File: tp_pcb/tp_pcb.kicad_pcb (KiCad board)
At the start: 2 copper layers, 66.5 x 76 mm, 23 parts, among them K0 KEYSW, K1 KEYSW, K2 KEYSW, K3 KEYSW, K4 KEYSW, K5 KEYSW, K6 KEYSW, P0 CONN_01X08, P1 CONN_01X08, P2 CONN_01X06

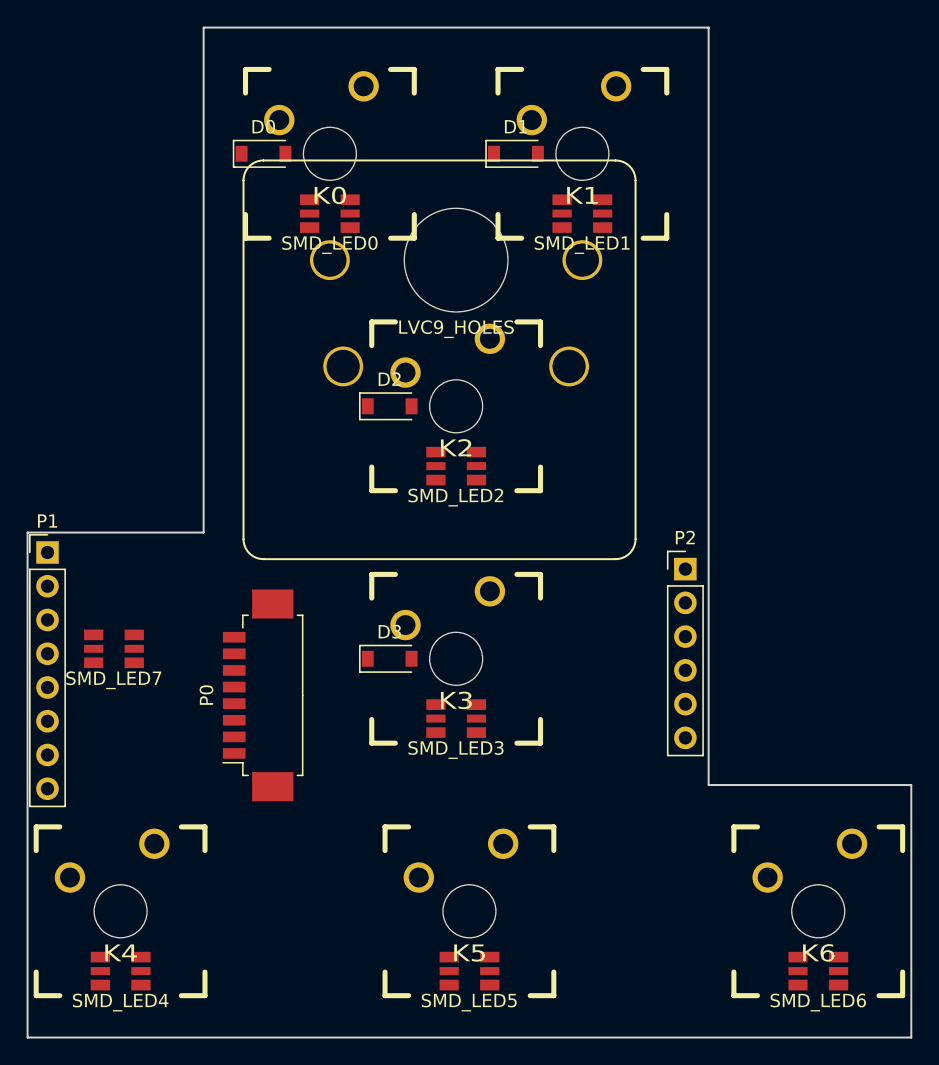
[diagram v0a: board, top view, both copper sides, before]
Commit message: tp_pcb routing, woo interactive
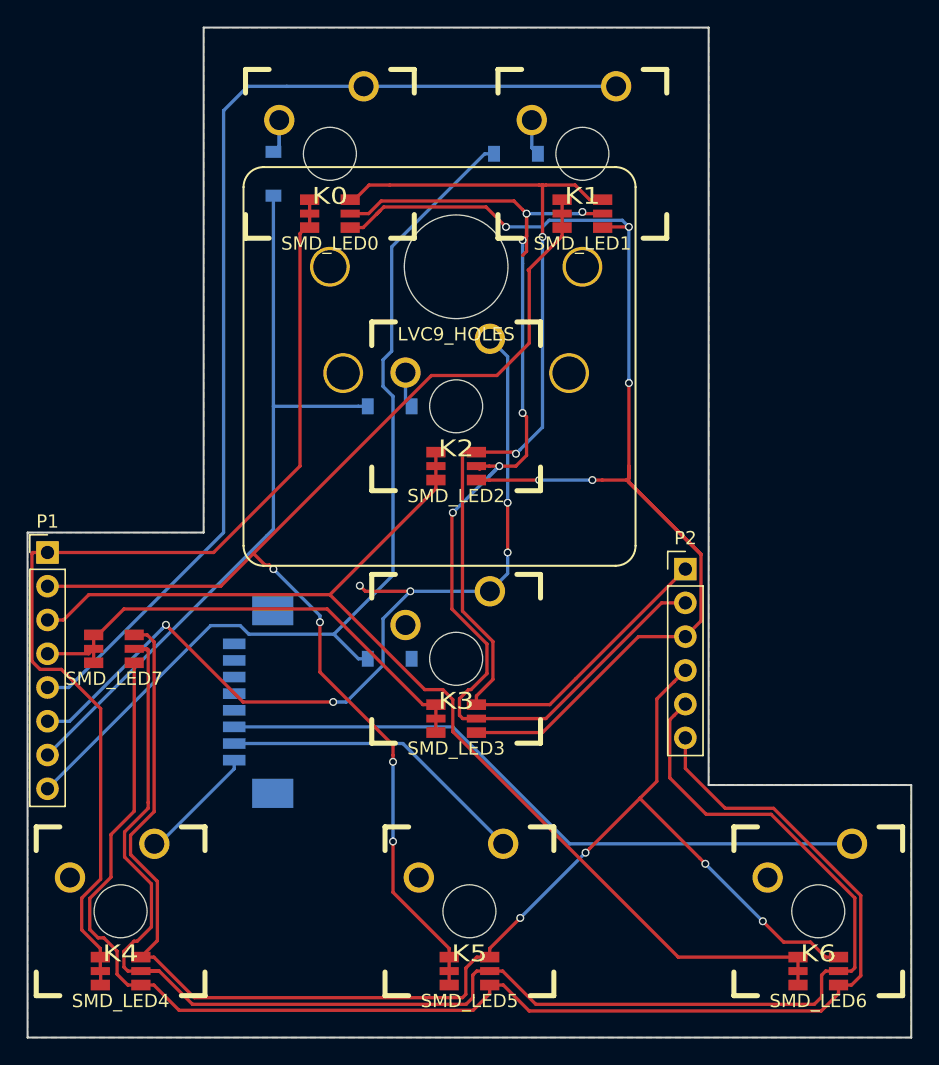
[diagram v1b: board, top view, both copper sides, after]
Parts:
- D0, D1, D2, D3, P0: moved to B.Cu
- moved D0 1.68 mm to (124.2, 44.5), turned to 90 degrees
- moved LVC9_HOLES 0.50 mm to (138.0, 51.5)
- moved P0 0.50 mm to (122.8, 84.2), turned to 270 degrees
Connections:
- D0 pad 1: Net-(D0-Pad1) -> c0
- D1 pad 1: Net-(D1-Pad1) -> c1
- D2 pad 1: Net-(D2-Pad1) -> c0
- D3 pad 1: Net-(D3-Pad1) -> c1
- P1 pad 5: Net-(P1-Pad5) -> r0
- P1 pad 6: Net-(P1-Pad6) -> r1
- P1 pad 7: Net-(P1-Pad7) -> c0
- P1 pad 8: Net-(P1-Pad8) -> c1
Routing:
- net red1: track 0.00 -> 120.3 mm
- net green1: track 0.00 -> 112.0 mm
- net blue1: track 0.00 -> 105.7 mm, vias 0 -> 4
- net green0: track 0.00 -> 97.8 mm, vias 0 -> 5
- net a1: track 0.00 -> 94.5 mm, vias 0 -> 4
- net red0: track 0.00 -> 89.8 mm, vias 0 -> 6
- net a2: track 0.00 -> 86.1 mm
- net blue0: track 0.00 -> 85.4 mm, vias 0 -> 2
- net a0: track 0.00 -> 80.6 mm
- net r0: track 0.00 -> 80.1 mm
- net c1: track 0.00 -> 72.4 mm
- net r1: track 0.00 -> 68.3 mm, vias 0 -> 6
- net c0: track 0.00 -> 56.5 mm
- net BTN2: track 0.00 -> 50.1 mm
- net a3: track 0.00 -> 37.4 mm
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- added copper zone on B.Cu, net GND
- added copper zone on F.Cu, net GND

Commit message: tp major improvements + routing, tp holes improved and modified
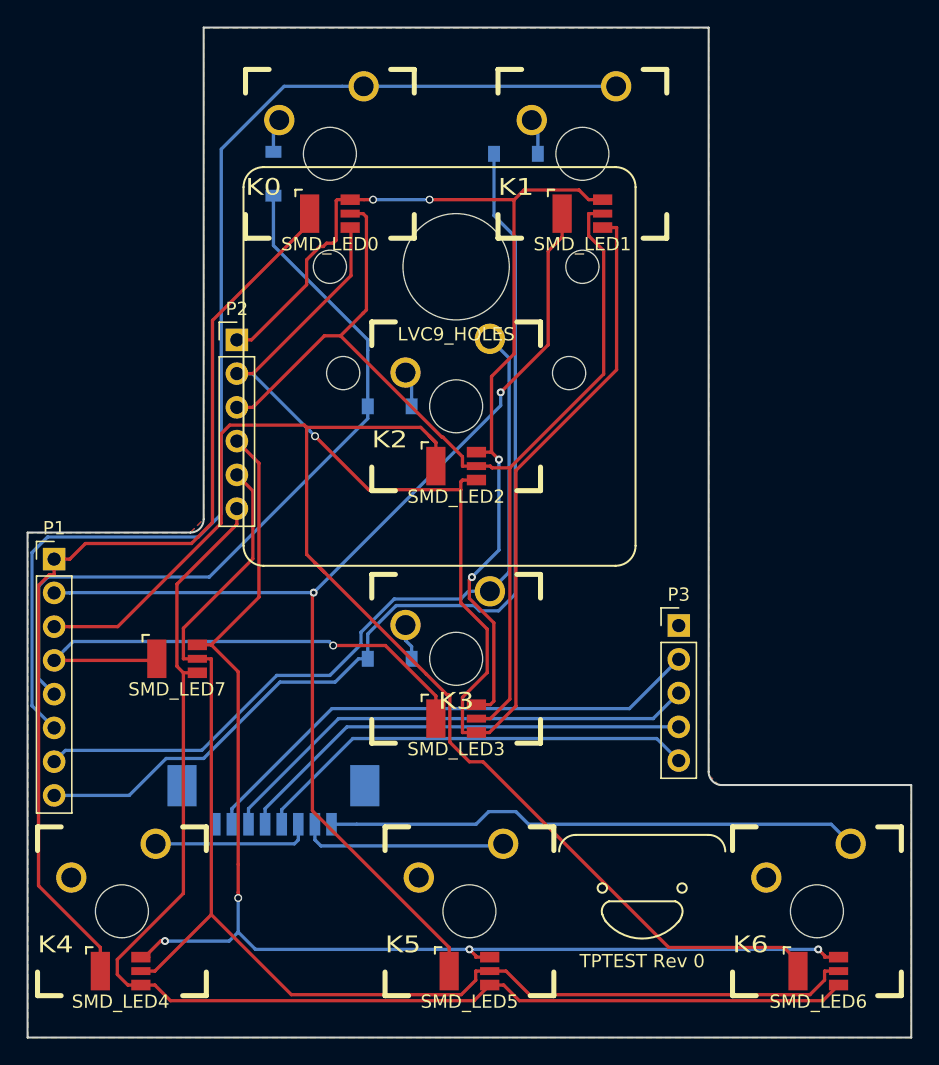
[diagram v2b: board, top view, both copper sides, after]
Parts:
- added P3: CONN_01X05, Socket_Strips:Socket_Strip_Straight_1x05_Pitch2.54mm, F.Cu at (154.8, 78.5)
- added TPTEST Rev 0: tgbugs_sig, cherry_rgb:tgbugs_sig, B.Cu at (152.0, 99.2)
- added TPTEST Rev 0: tgbugs_sig, cherry_rgb:tgbugs_sig, F.Cu at (152.0, 99.2)
- SMD_LED0, SMD_LED1, SMD_LED2, SMD_LED3, SMD_LED4, SMD_LED5, SMD_LED6, SMD_LED7: footprint cherry_rgb:SMLVN6RGB -> cherry_rgb:SMLVN6RGB_CA
- moved P2 37.9 mm to (121.5, 57.0)
- moved P0 7.89 mm to (124.2, 92.0), turned to 0 degrees
- moved SMD_LED7 4.81 mm to (117.0, 81.0)
- moved P1 0.71 mm to (107.8, 73.5)
- moved K4 0.10 mm to (112.8, 100.0)
- moved K6 0.10 mm to (165.2, 100.0)
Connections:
- P0 pad 6: BTN2 -> BTN0
- P0 pad 8: BTN0 -> BTN2
- P1 pad 5: r0 -> c0
- P1 pad 6: r1 -> r0
- P1 pad 7: c0 -> r1
- P2 pad 2: red0 -> green0
- P2 pad 3: green0 -> red0
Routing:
- net RST: track 0.00 -> 39.5 mm
- net VCC: track 0.00 -> 37.2 mm
- net DATA: track 0.00 -> 34.8 mm
- net CLK: track 0.00 -> 33.9 mm
- net red1: track 120.3 -> 97.6 mm
- net a2: track 86.1 -> 105.0 mm
- net green1: track 112.0 -> 96.8 mm
- net BTN2: track 50.1 -> 40.5 mm
- net r1: track 68.3 -> 58.8 mm, vias 6 -> 0
- net r0: track 80.1 -> 88.5 mm
- net blue1: track 105.7 -> 97.6 mm
- net BTN1: track 23.4 -> 15.6 mm
- net a0: track 80.6 -> 73.0 mm
- net red0: track 89.8 -> 82.5 mm, vias 6 -> 0
- net blue0: track 85.4 -> 78.2 mm, vias 2 -> 4
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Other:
- outline, holes or cut-outs redrawn
